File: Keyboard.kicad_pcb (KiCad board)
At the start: 2 copper layers, 404 x 118.3 mm, 226 parts, among them SW2 RotaryEncoder_Switch_MP, U1 MCP23017_SO, U2 MCP23017_SO, U3 Seeeduino Xiao nRF52840

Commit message: Minor update.
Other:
- board text added: "JLCJLCJLCJLC"
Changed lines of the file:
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@@
 		(layer "Edge.Cuts")
+	)
+	(gr_text "JLCJLCJLCJLC"
+		(at 177.8 132.08 0)
+		(layer "F.SilkS")
+		(effects
+			(font
+				(size 3 3)
+				(thickness 0.5)
+				(bold yes)
+			)
+			(justify left bottom)
+		)
 	)
 	(gr_text "18x17 spacing"

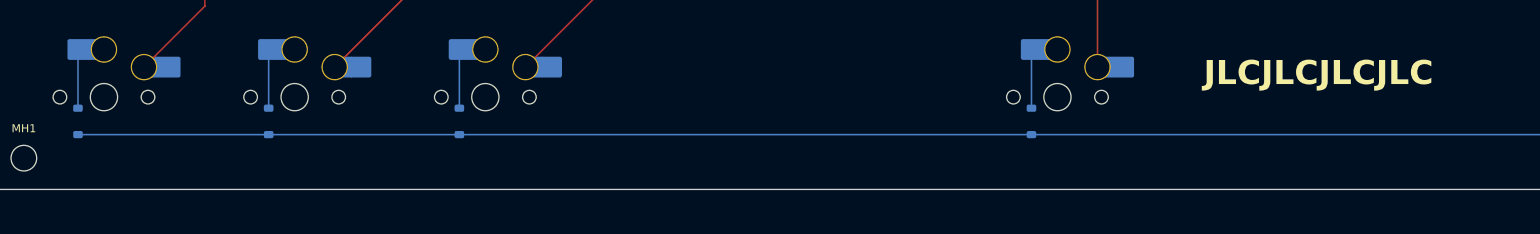
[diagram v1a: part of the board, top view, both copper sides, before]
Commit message: Added text to the pcb.
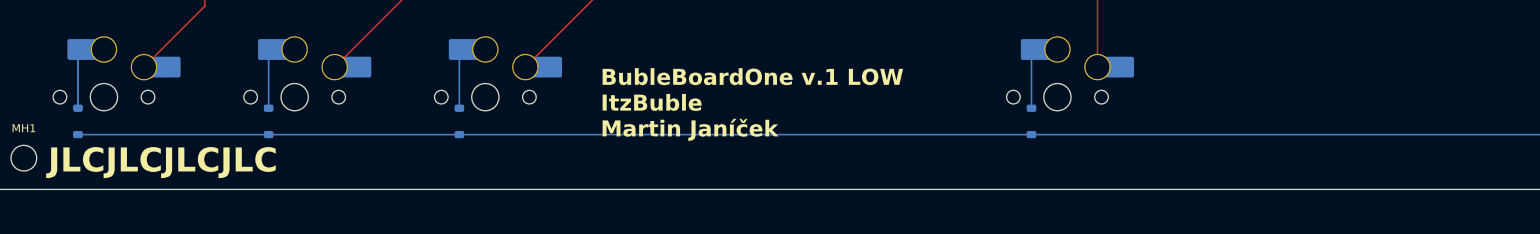
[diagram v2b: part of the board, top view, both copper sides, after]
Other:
- board text added: "BubleBoardOne v.1 LOW ItzBuble Martin Janíček"
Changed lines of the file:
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@@
 		(layer "Edge.Cuts")
 	)
-	(gr_text "JLCJLCJLCJLC"
-		(at 177.8 132.08 0)
+	(gr_text "BubleBoardOne v.1 LOW\nItzBuble\nMartin Janíček"
+		(at 102.5 138.5 0)
 		(layer "F.SilkS")
 		(effects
+			(font
+				(size 2 2)
+				(thickness 0.4)
+				(bold yes)
+			)
+			(justify left bottom)
+		)
+	)
+	(gr_text "JLCJLCJLCJLC"
+		(at 33.5 143 0)
+		(layer "F.SilkS")
+		(effects
